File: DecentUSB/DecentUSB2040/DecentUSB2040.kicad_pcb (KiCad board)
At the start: 2 copper layers, 97.2 x 58.9 mm, 128 parts, among them J1 USB_B_Micro, J10 SM03B-SRSS-TB, J11 Conn_01x04, J2 Conn_01x08, J3 Conn_01x08, J5 Conn_02x09_Counter_Clockwise, J6 Conn_02x05_Odd_Even, J7 Conn_01x08, J8 Conn_01x03, J9 Conn_01x04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

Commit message: DecentUSB Host 2040 rev. 3
Now using the already available RP2040 MCU
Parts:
- D2: footprint LED_SMD:LED_WS2812B_PLCC4_5.0x5.0mm_P3.2mm -> DecenTKL:WS2812C
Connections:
- U1 pad 31: unconnected-(U1-IO19-Pad31) -> NeoPixelData
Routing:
- net NeoPixelData: track 0.00 -> 20.5 mm, vias 0 -> 2
- net Net-(D2-DOUT): track 14.8 -> 9.65 mm
- net +5V: track 88.1 -> 85.2 mm
- net +3V3: track 269.9 -> 267.7 mm
- net GND: track 505.6 -> 504.3 mm
- net ~{K2}: track 8.55 -> 8.05 mm

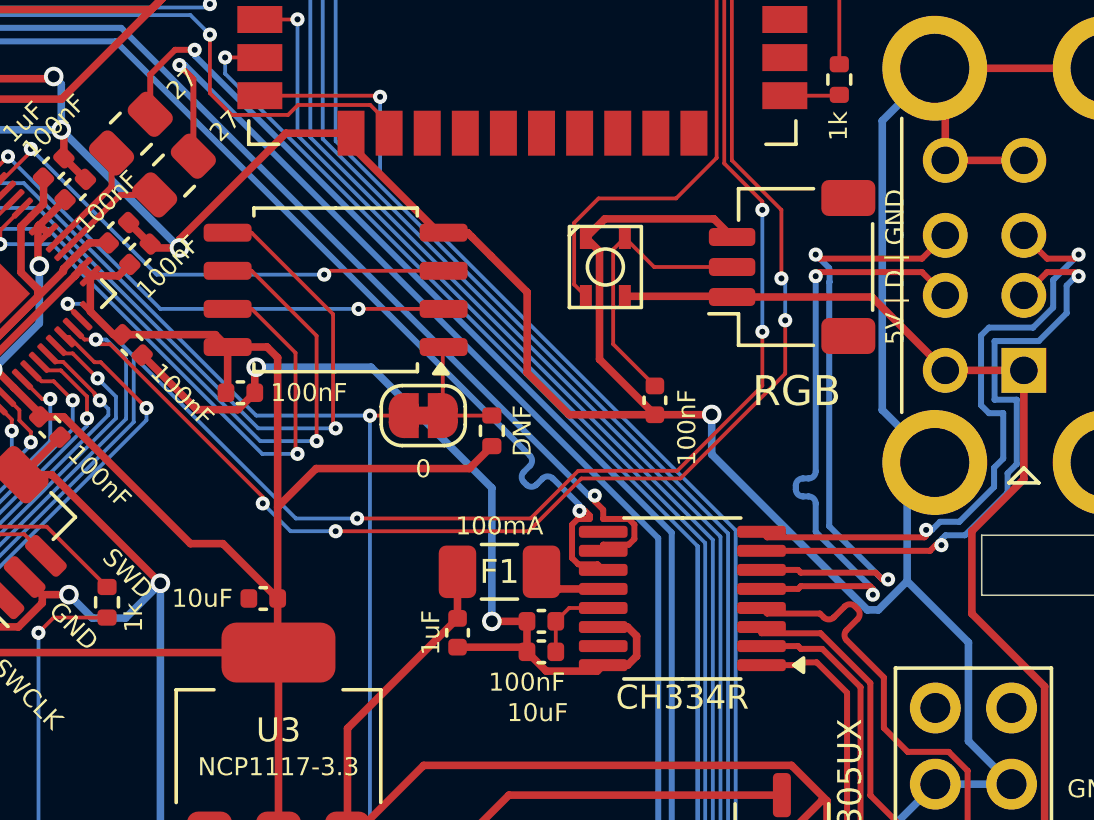
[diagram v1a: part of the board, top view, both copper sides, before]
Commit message: Small production adjustment to DecentUSB 2040
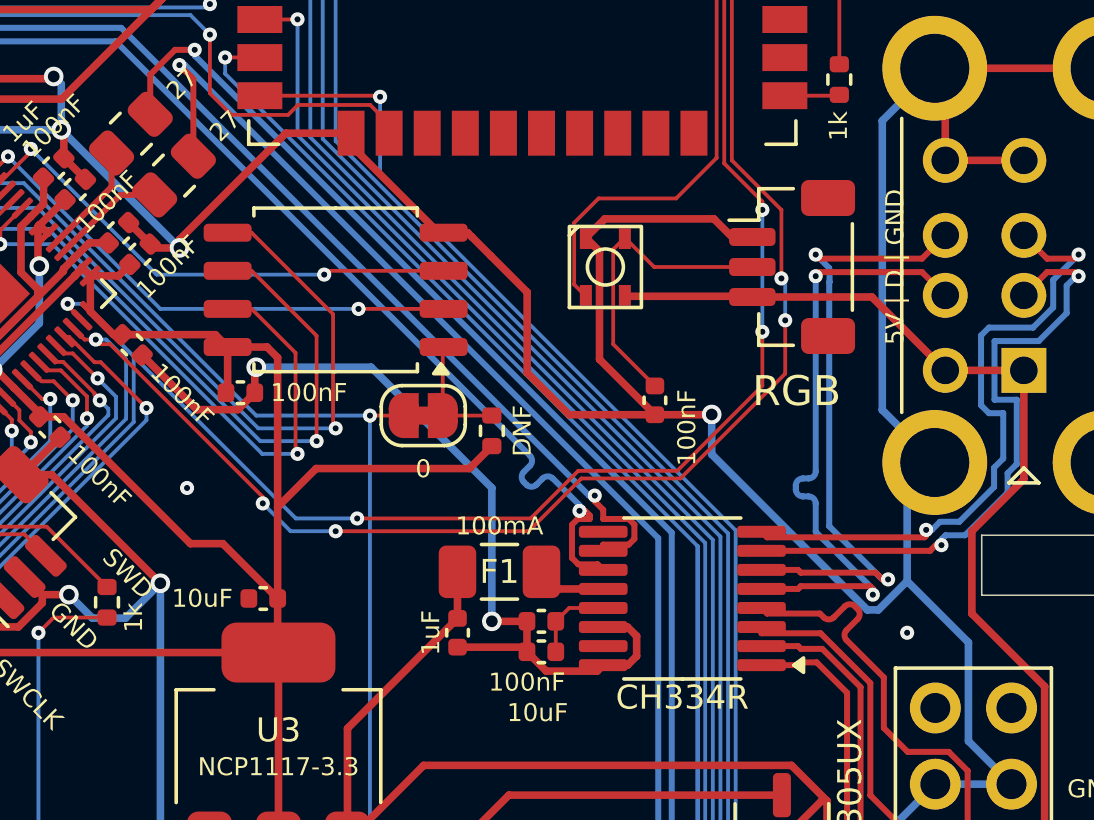
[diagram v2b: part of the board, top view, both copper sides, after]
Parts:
- J8: footprint Connector_JST:JST_SH_SM03B-SRSS-TB_1x03-1MP_P1.00mm_Horizontal -> Connector_JST:JST_SH_BM03B-SRSS-TB_1x03-1MP_P1.00mm_Vertical
- turned J8 to -90 degrees
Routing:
- net GND: vias 32 -> 34

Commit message: DecentUSB 2040 adjustments
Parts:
- moved H1 31.8 mm to (218.4, 87.0)
- moved C38 28.7 mm to (187.2, 69.8), turned to 180 degrees
- moved J9 27.8 mm to (165.3, 72.7)
- moved C39 27.2 mm to (185.3, 69.8)
- moved C41 25.8 mm to (182.9, 69.8), turned to 180 degrees
- moved R36 24.3 mm to (174.0, 69.8)
- moved C40 23.1 mm to (180.3, 69.8)
- moved SW4 22.1 mm to (164.8, 86.6), turned to 90 degrees
- moved R11 10.3 mm to (167.1, 70.1), turned to 180 degrees
- moved U1 9.60 mm to (179.0, 80.2), turned to -90 degrees
- moved C20 8.21 mm to (165.1, 70.1), turned to 180 degrees
- moved J11 7.56 mm to (129.8, 96.3)
- moved H3 2.00 mm to (134.3, 100.6)
- moved J8 2.00 mm to (177.7, 99.1)
- moved USB1-2 2.00 mm to (185.4, 102.5)
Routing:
- net +3V3: track 267.7 -> 214.6 mm, vias 11 -> 12
- net GND: track 504.3 -> 454.2 mm, vias 34 -> 35
- net /~{ESP32_BOOT_SEL}: track 18.1 -> 0.00 mm
- net ESP32_RX: track 17.5 -> 0.00 mm
- net RESET3V3: track 147.7 -> 132.4 mm, vias 2 -> 1
- net ESP32_TX: track 14.9 -> 0.00 mm
- net OPTION3V3: track 143.3 -> 131.0 mm, vias 2 -> 1
- net NeoPixelData: track 20.5 -> 8.26 mm, vias 2 -> 0
- net I2C_SCL: track 94.5 -> 83.0 mm, vias 5 -> 4
- net SELECT3V3: track 137.6 -> 127.0 mm, vias 2 -> 1
- net Net-(U1-EN): track 9.97 -> 0.00 mm
- net I2C_SDA: track 92.4 -> 85.0 mm, vias 6 -> 5
- net START3V3: track 132.8 -> 126.5 mm, vias 2 -> 1
- net J2:POTA: track 56.3 -> 52.8 mm
- net J2:POTB: track 54.0 -> 51.5 mm
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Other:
- outline, holes or cut-outs redrawn
- board text added: "Rev. 4"
- board text removed: "Rev. 3"
